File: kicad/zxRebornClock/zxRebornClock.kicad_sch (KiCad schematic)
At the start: 98 parts, among them J1 Conn_01x04, J2 Conn_01x03, J3 USB_B_Micro, J4 Conn_01x03, J5 Jack DC, J6 Conn_01x02, Q1 MMBTA42, Q11 MMBTA42, Q2 MMBTA42, Q3 MMBTA42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

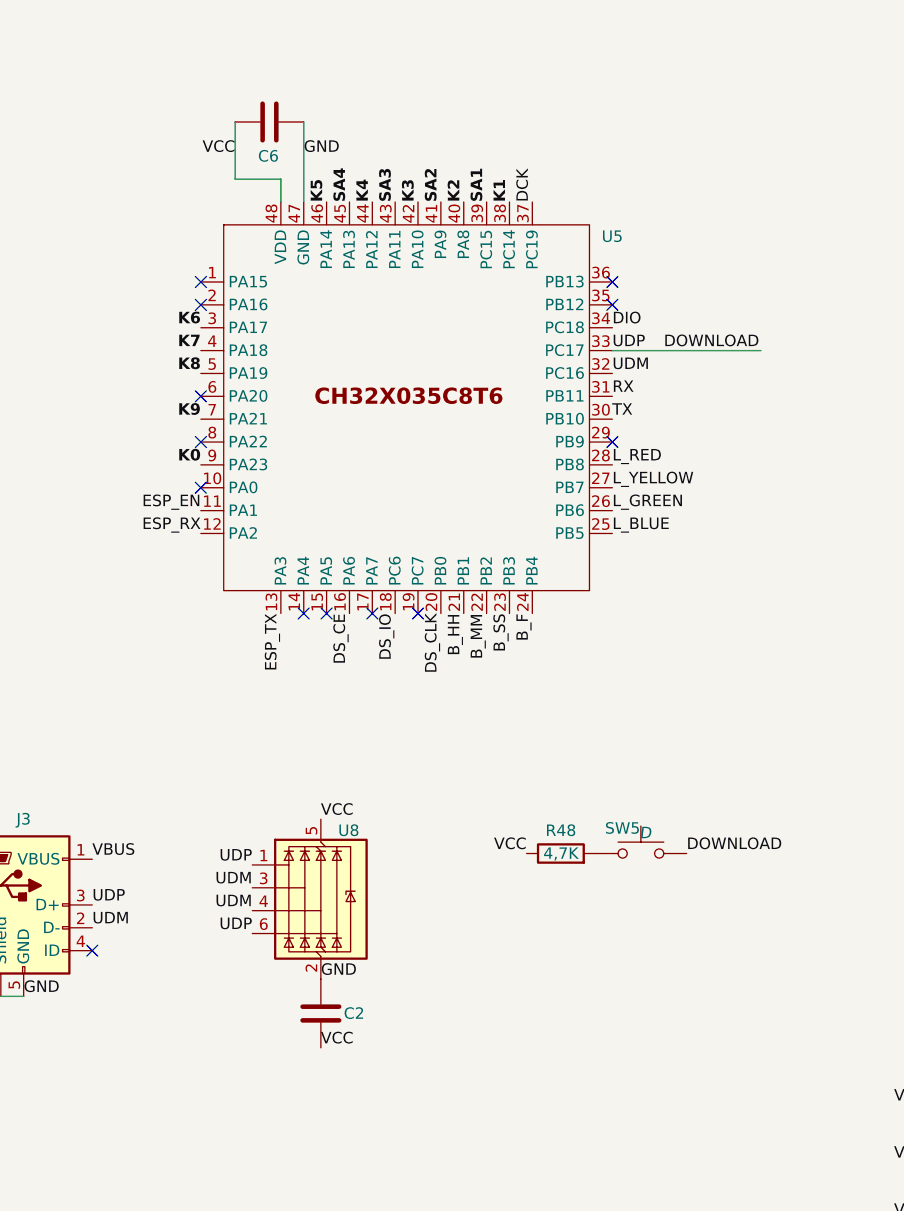
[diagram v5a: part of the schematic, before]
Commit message: add rst button
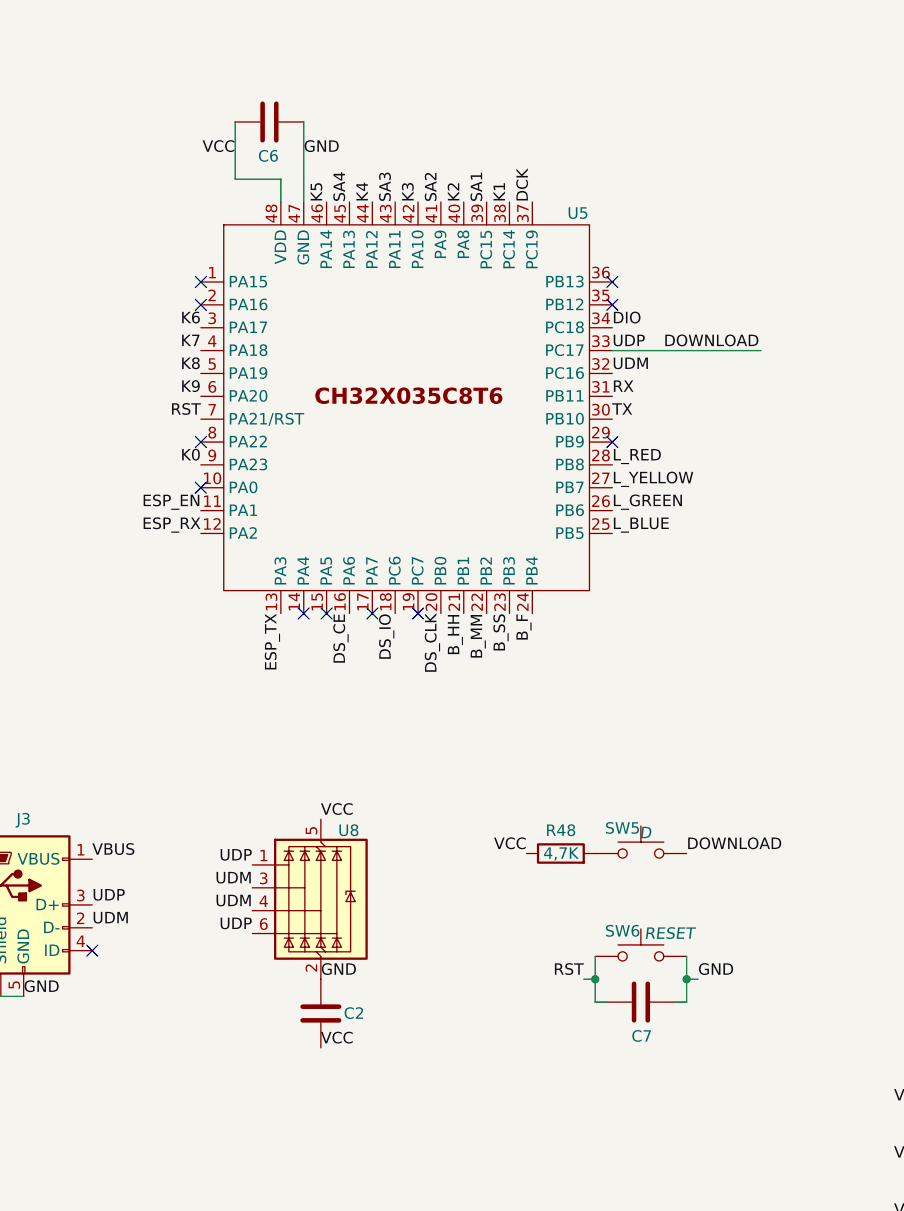
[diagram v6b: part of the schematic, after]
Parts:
- added C7: C, symbol Device:C
- added SW6: RESET, symbol Switch:SW_Push
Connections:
- net GND: now also C7.2, SW6.2
- net K9: now also U5.6 (PA20); no longer U5.7 (PA21)
- new net RST: C7.1, SW6.1, U5.7 (PA21/RST)
- no-connect marks 34 -> 33

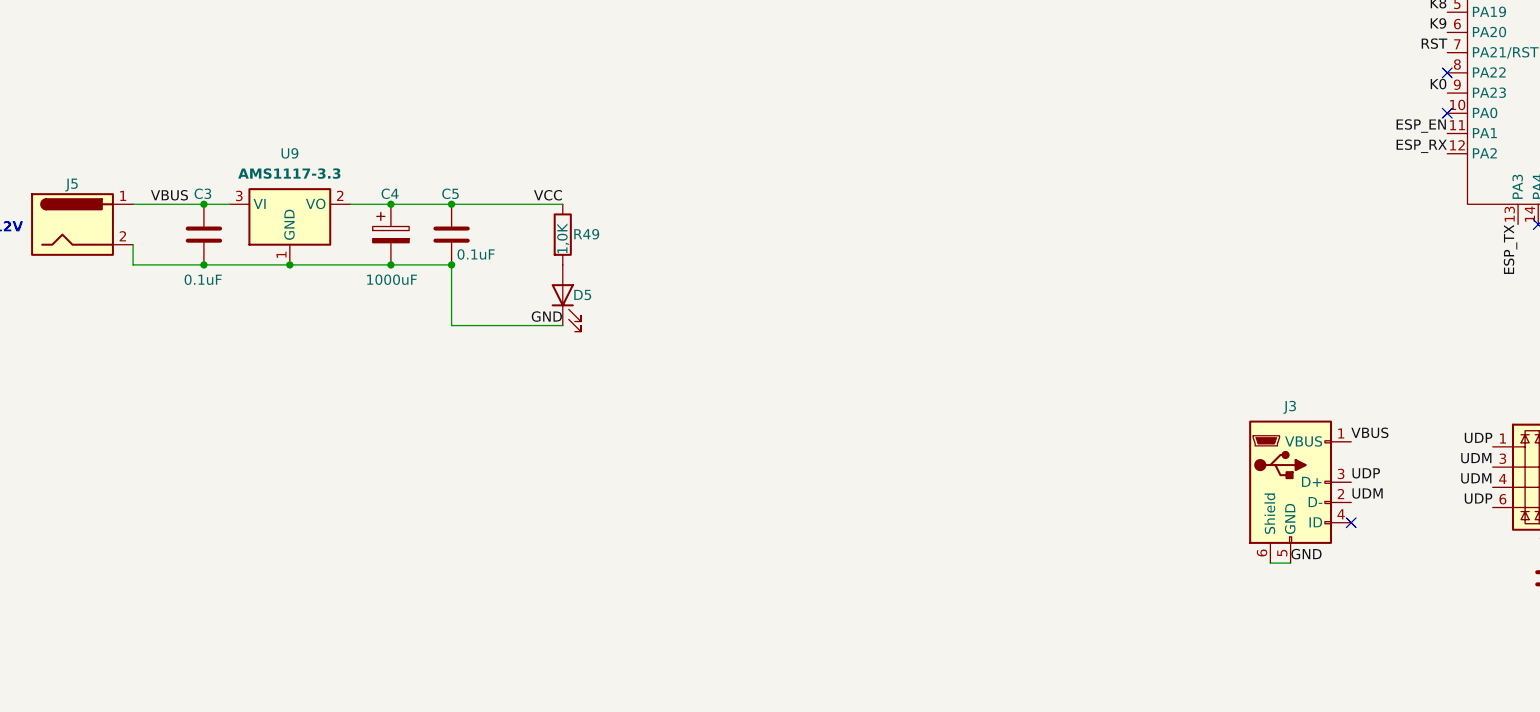
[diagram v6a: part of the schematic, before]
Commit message: add 12V->200V
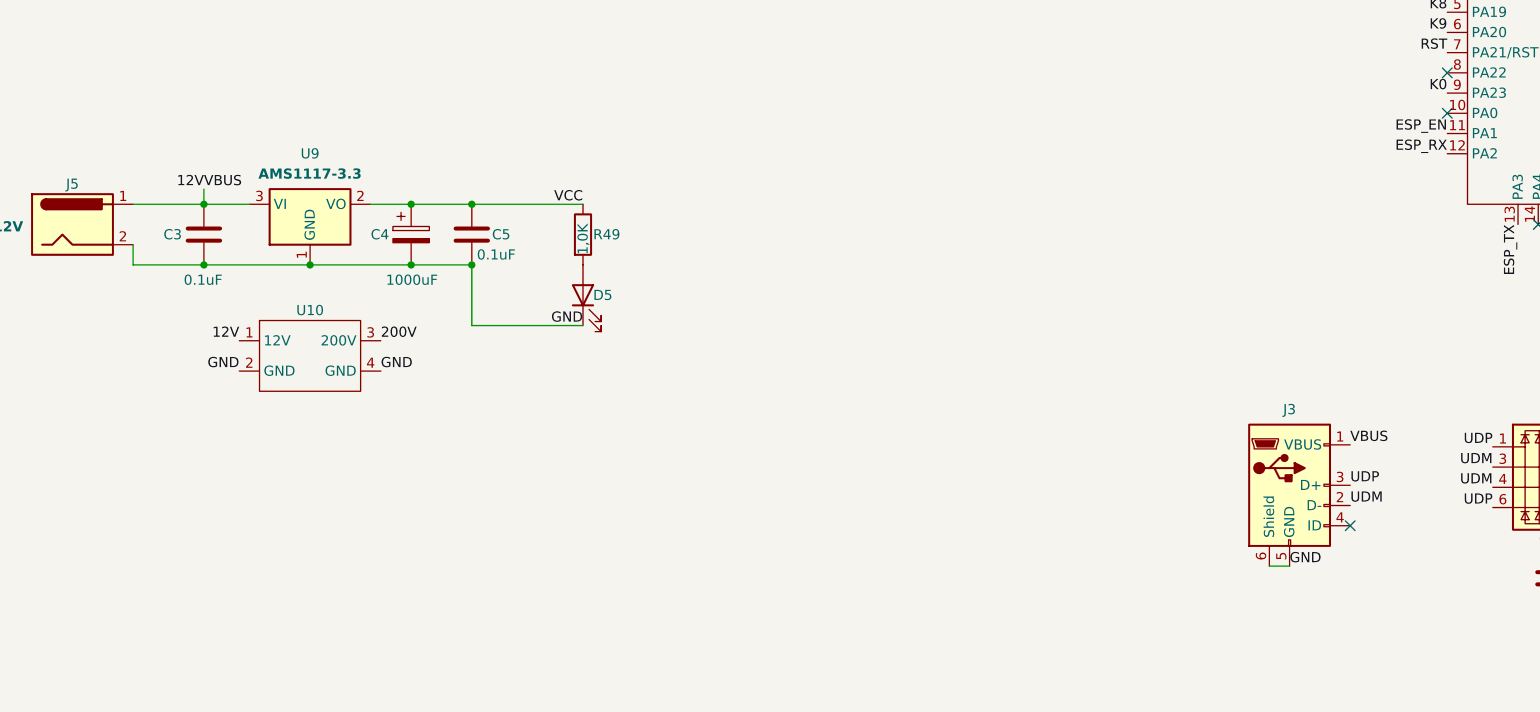
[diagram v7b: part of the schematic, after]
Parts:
- added U10: ~, symbol in14-clock:12V_to_200V
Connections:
- net 200V: now also U10.3 (200V)
- net GND: now also U10.2 (GND), U10.4 (GND)
- net VBUS renamed 12V
- net 12V: now also U10.1 (12V)
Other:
- moved on the sheet: C4, C5, D5, R49, U9

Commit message: fix border
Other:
- note added: "zxRebornClock"
- note added: "часы на газоразрядных лампах ИН-14"
- company: (none) -> https://t.me/emacser2015
- title: (none) -> zxRebornClock (часы на газоразрядных лампах ИН-14)
- moved on the sheet: BT1, C1, C2, C3, C4, C5, C6, C7, D1, D2, D3, D4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
